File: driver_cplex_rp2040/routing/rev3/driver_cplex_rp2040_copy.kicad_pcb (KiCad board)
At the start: 6 copper layers, 40.2 x 40.2 mm, 479 parts, among them J1 Conn_01x05, J2 Conn_01x05, J3 Conn_01x05, J4 Conn_01x05, J5 Conn_01x04, Q1 1xPNP and 1xNPN, Q10 1xPNP and 1xNPN, Q11 1xPNP and 1xNPN, Q12 1xPNP and 1xNPN, Q13 1xPNP and 1xNPN, Q14 1xPNP and 1xNPN, Q15 1xPNP and 1xNPN, Q16 1xPNP and 1xNPN, Q17 1xPNP and 1xNPN, Q18 1xPNP and 1xNPN, Q19 1xPNP and 1xNPN, Q2 1xPNP and 1xNPN, Q20 1xPNP and 1xNPN, Q21 1xPNP and 1xNPN, Q22 1xPNP and 1xNPN, Q23 1xPNP and 1xNPN, Q24 1xPNP and 1xNPN, Q25 1xPNP and 1xNPN, Q26 1xPNP and 1xNPN, Q27 1xPNP and 1xNPN, Q28 1xPNP and 1xNPN, Q29 1xPNP and 1xNPN, Q3 1xPNP and 1xNPN, Q30 1xPNP and 1xNPN, Q31 1xPNP and 1xNPN, Q32 1xPNP and 1xNPN, Q33 1xPNP and 1xNPN, Q34 1xPNP and 1xNPN, Q4 1xPNP and 1xNPN, Q5 1xPNP and 1xNPN, Q6 1xPNP and 1xNPN, Q7 1xPNP and 1xNPN, Q8 1xPNP and 1xNPN, Q9 1xPNP and 1xNPN, SW1 SW_Push, SW2 SW_Push, U1 AP2112K-3.3, U2 RP2040, U3 W25Q16JVUXIQ_TR, Y1 12MHz

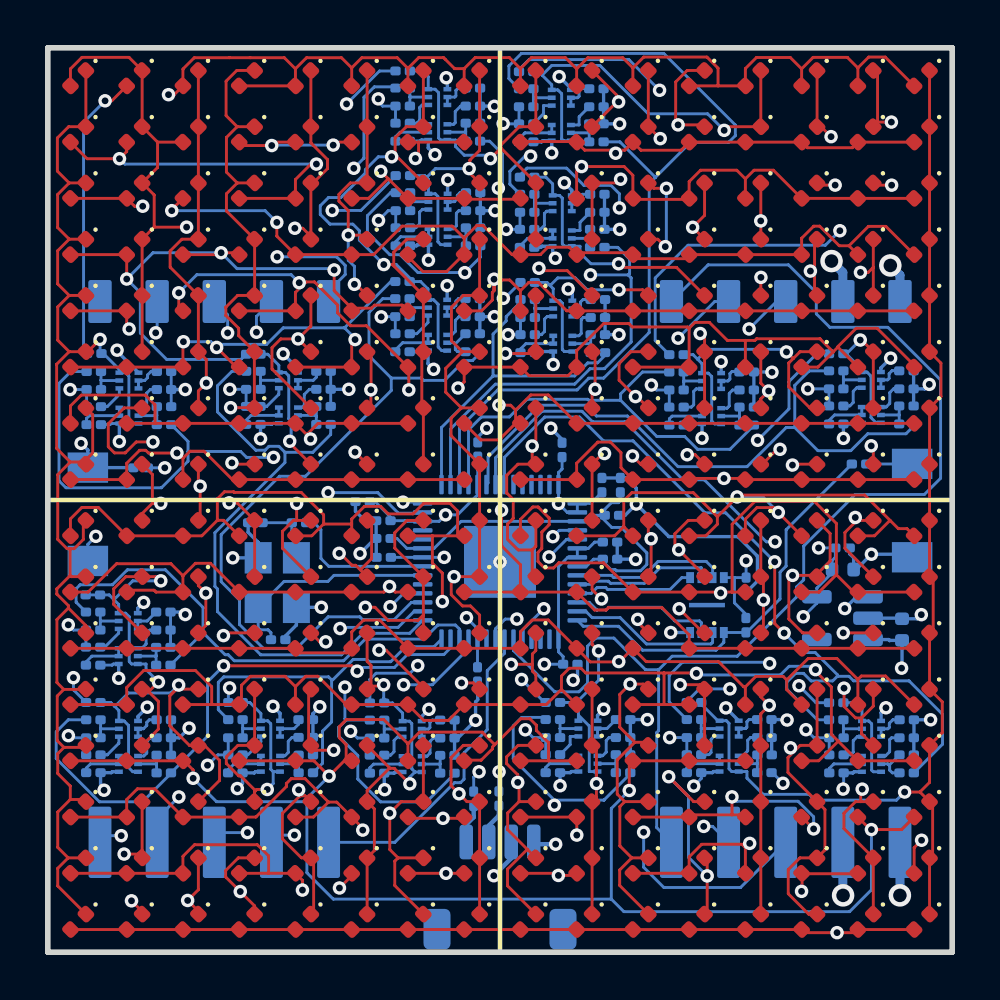
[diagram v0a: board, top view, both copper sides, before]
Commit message: Completed initial routing.
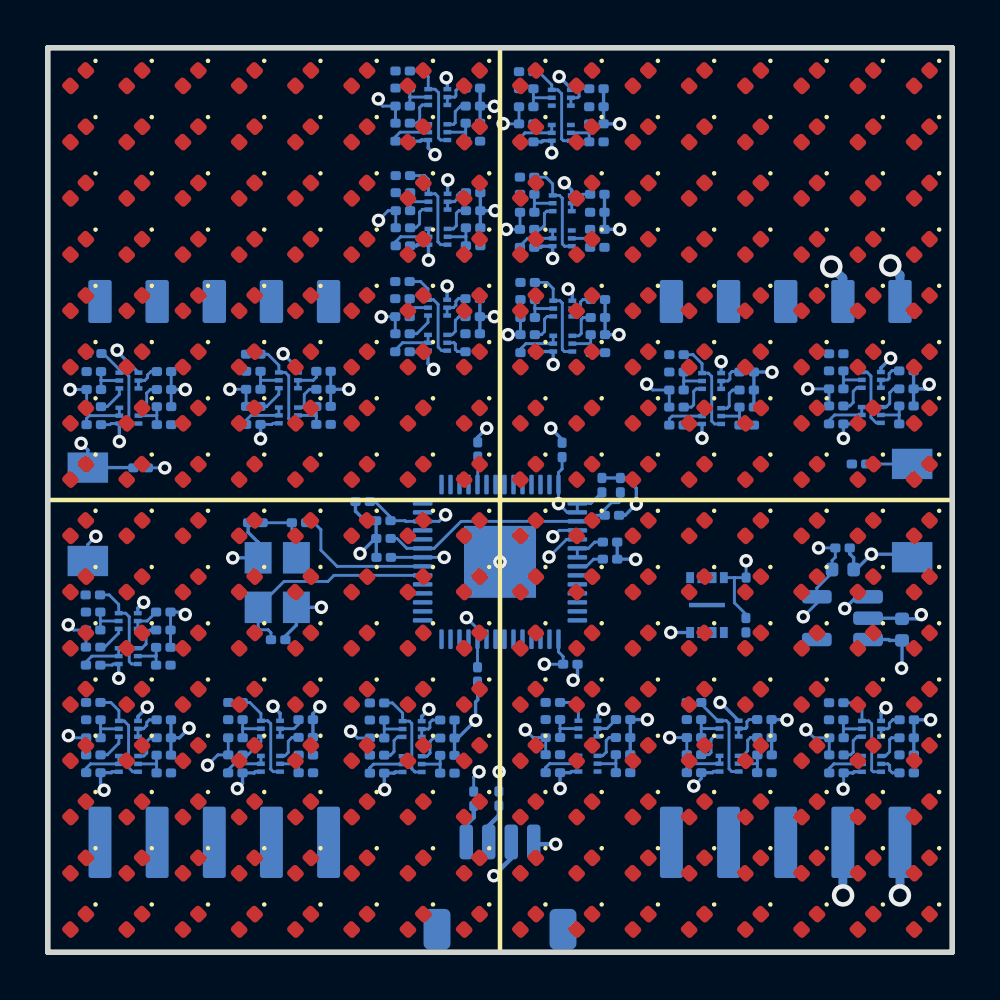
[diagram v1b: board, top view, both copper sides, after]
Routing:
- net Net-(D109-A): track 124.6 -> 0.00 mm, vias 5 -> 0
- net /level_shifter/CP_5V_01: track 124.5 -> 4.35 mm, vias 11 -> 0
- net Net-(D104-A): track 105.3 -> 0.00 mm, vias 4 -> 0
- net Net-(D105-A): track 103.6 -> 0.00 mm, vias 3 -> 0
- net Net-(D103-A): track 92.2 -> 0.00 mm, vias 3 -> 0
- net Net-(D108-A): track 90.0 -> 0.00 mm, vias 3 -> 0
- net /level_shifter/CP_5V_08: track 90.5 -> 4.45 mm, vias 5 -> 0
- net Net-(D115-A): track 84.3 -> 0.00 mm, vias 5 -> 0
- net Net-(D110-A): track 83.5 -> 0.00 mm, vias 7 -> 0
- net /level_shifter/CP_5V_06: track 83.7 -> 4.33 mm, vias 5 -> 0
- net Net-(D102-A): track 75.2 -> 0.00 mm, vias 6 -> 0
- net Net-(D107-A): track 73.0 -> 0.00 mm, vias 2 -> 0
- net /level_shifter/CP_5V_07: track 76.9 -> 4.49 mm, vias 4 -> 0
- net Net-(D10-A): track 72.2 -> 0.00 mm, vias 3 -> 0
- net /level_shifter/CP_5V_11: track 76.1 -> 4.43 mm, vias 10 -> 0
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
